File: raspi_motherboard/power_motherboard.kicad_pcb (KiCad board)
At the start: 4 copper layers, 65 x 59.5 mm, 61 parts, among them J1 GPIO, J2 Conn_02x04_Top_Bottom, J3 Conn_01x03, U1 MCP2515-xST, U2 SN65HVD230, U3 TPS563200, Y1 AMB8-12Mhz

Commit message: Add logo
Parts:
- added G***: LOGO, powerboard:krabi, F.Cu at (150.5, 94.0)
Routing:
- net GND_ELEC: vias 40 -> 41

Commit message: small fixes
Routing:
- net 12V_POW_P: track 59.4 -> 54.2 mm
- net Net-(D_12VE_INV1-K): track 21.8 -> 19.4 mm
- net GND_ELEC: track 262.8 -> 260.7 mm, vias 41 -> 49
- net 12V_ELEC_P: track 164.8 -> 162.7 mm
- net GND_POW: vias 10 -> 16
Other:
- board size 65 x 59.5 mm -> 65 x 59.9 mm

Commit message: Update
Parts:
- removed GPIO16: Conn_01x04_Socket, Connector_PinSocket_2.54mm:PinSocket_1x04_P2.54mm_Vertical
- added Tir&B: Conn_01x04_Socket, Connector_PinSocket_2.54mm:PinSocket_1x04_P2.54mm_Vertical, F.Cu at (162.8, 58.2)
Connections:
- J1 pad 38: /GPIO20/PCM.DIN -> R_IO20
- J1 pad 40: /GPIO21/PCM.DOUT -> R_IO21
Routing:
- net R_IO16: track 19.4 -> 41.8 mm
- net R_IO20: track 0.00 -> 19.0 mm
- net R_IO21: track 0.00 -> 14.4 mm
- net 3_3V: track 95.0 -> 88.5 mm
- net 5V: track 114.8 -> 108.3 mm
- net GND_ELEC: track 260.7 -> 260.2 mm, vias 49 -> 47
- net GND_POW: vias 16 -> 15

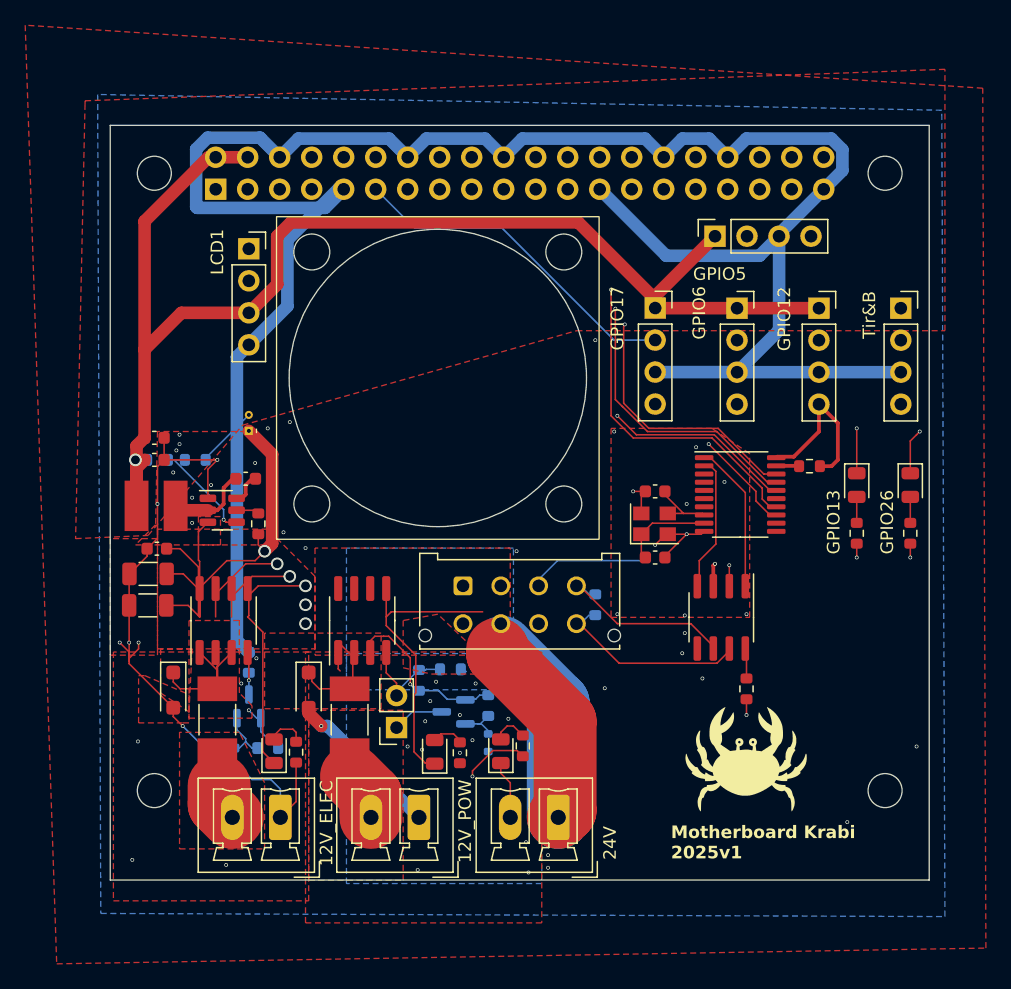
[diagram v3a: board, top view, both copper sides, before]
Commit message: fix ERC/DRC (including short-circuits) + add flood fills
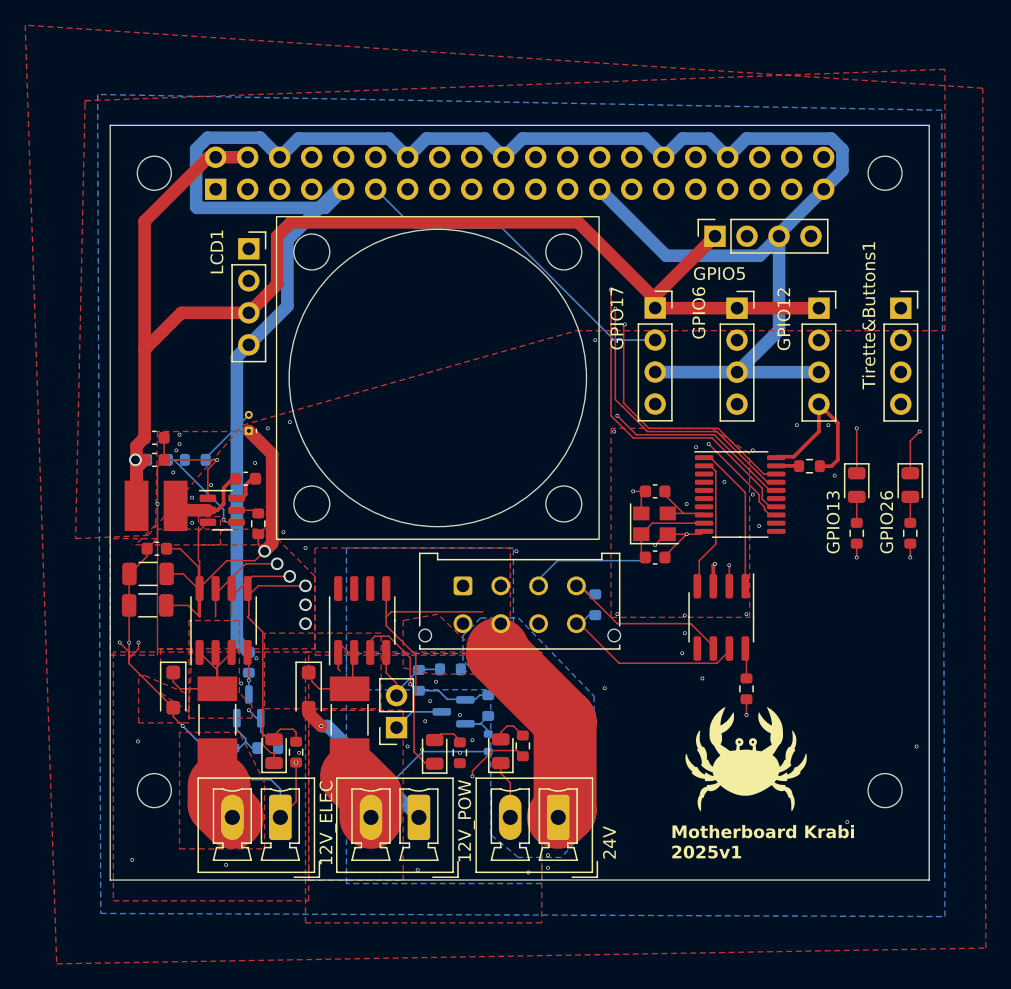
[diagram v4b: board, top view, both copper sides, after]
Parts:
- renumbered Tir&B to Tirette&Buttons1
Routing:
- net R_IO16: track 41.8 -> 22.5 mm
- net R_IO20: track 19.0 -> 38.1 mm
- net 12V_POW_P: track 54.2 -> 38.9 mm
- net 24V_POW_P: track 34.5 -> 21.9 mm
- net GND_POW: track 21.2 -> 30.3 mm, vias 15 -> 12
- net GND_ELEC: track 260.2 -> 253.7 mm, vias 47 -> 55
- added copper zone on B.Cu, net 12V_POW_P
- added copper zone on In1.Cu, net 24V_POW_P
- added copper zone on In1.Cu, net GND_ELEC
- added copper zone on In2.Cu, net GND_ELEC

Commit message: Fix double line + priority
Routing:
- net R_IO20: track 38.1 -> 19.2 mm
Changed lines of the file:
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@@
 				(polygon
 					(pts
-						(xy 111.601737 68.119259) (xy 111.499644 68.119259) (xy 111.499644 67.780494) (xy 111.601737 67.780494)
+						(xy 111.42979 67.791973) (xy 111.617369 67.791973) (xy 111.617369 68.105826) (xy 111.42979 68.105826)
 					)
 				)
@@
 	)
 	(segment
-		(start 155.1305 49.3805)
-		(end 155.1305 48.33901)
+		(start 152.82 47.5)
+		(end 151.55 46.23)
 		(width 0.127)
 		(layer "In1.Cu")
@@
 	)
 	(segment
-		(start 152.5905 47.2705)
-		(end 151.55 46.23)
+		(start 157.4165 51.6665)
+		(end 155.25 49.5)
 		(width 0.127)
 		(layer "In1.Cu")
@@
 	)
 	(segment
-		(start 157.4165 51.6665)
-		(end 155.1305 49.3805)
+		(start 157.4165 58.2065)
+		(end 157.4165 51.6665)
 		(width 0.127)
 		(layer "In1.Cu")
@@
 	)
 	(segment
-		(start 155.1305 48.33901)
-		(end 154.06199 47.2705)
+		(start 155.25 48)
+		(end 154.75 47.5)
 		(width 0.127)
 		(layer "In1.Cu")
@@
 	)
 	(segment
-		(start 157.4165 58.2065)
-		(end 157.4165 51.6665)
+		(start 162.5 63.29)
+		(end 157.4165 58.2065)
 		(width 0.127)
 		(layer "In1.Cu")
@@
 	)
 	(segment
-		(start 154.06199 47.2705)
-		(end 152.5905 47.2705)
+		(start 154.75 47.5)
+		(end 152.82 47.5)
 		(width 0.127)
 		(layer "In1.Cu")
@@
 	)
 	(segment
-		(start 162.5 63.29)
-		(end 157.4165 58.2065)
+		(start 155.25 49.5)
+		(end 155.25 48)
 		(width 0.127)
 		(layer "In1.Cu")
@@
 	)
 	(segment
-		(start 156.75 47.2705)
-		(end 155.1305 47.2705)
-		(width 0.127)
-		(layer "In1.Cu")
-		(net 25)
-	)
-	(segment
-		(start 155.1305 47.2705)
-		(end 154.09 46.23)
-		(width 0.127)
-		(layer "In1.Cu")
-		(net 25)
-	)
-	(segment
-		(start 157.6705 55.9205)
-		(end 157.6705 48.191)
-		(width 0.127)
-		(layer "In1.Cu")
-		(net 25)
-	)
-	(segment
-		(start 162.5 60.75)
-		(end 157.6705 55.9205)
-		(width 0.127)
-		(layer "In1.Cu")
-		(net 25)
-	)
-	(segment
-		(start 157.6705 48.191)
-		(end 156.75 47.2705)
-		(width 0.127)
-		(layer "In1.Cu")
-		(net 25)
-	)
-	(segment
 		(start 154.5 50.65149)
 		(end 153.0495 49.20099)
@@
 		(layer "In1.Cu")
 		(hatch edge 0.5)
-		(priority 5)
 		(connect_pads yes
 			(clearance 0)

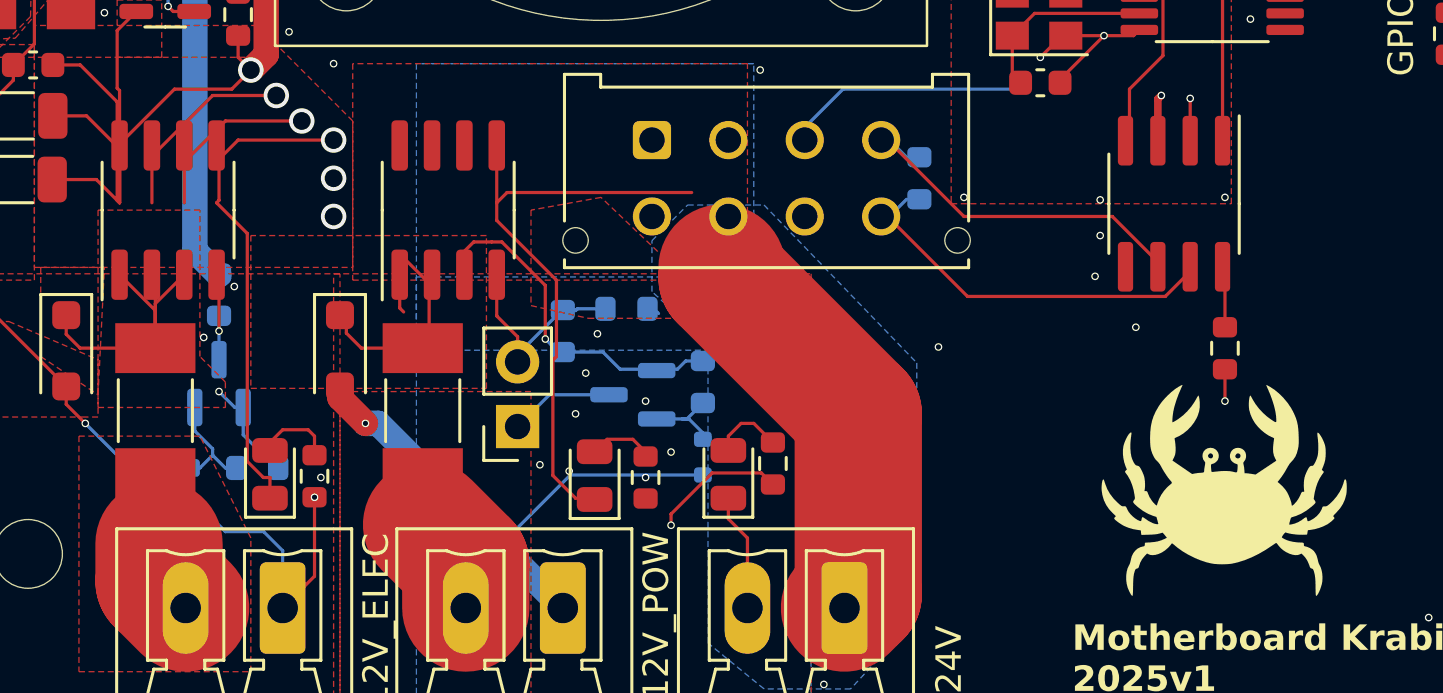
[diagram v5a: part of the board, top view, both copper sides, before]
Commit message: fix antennas (mainly on internal copper) + add labels
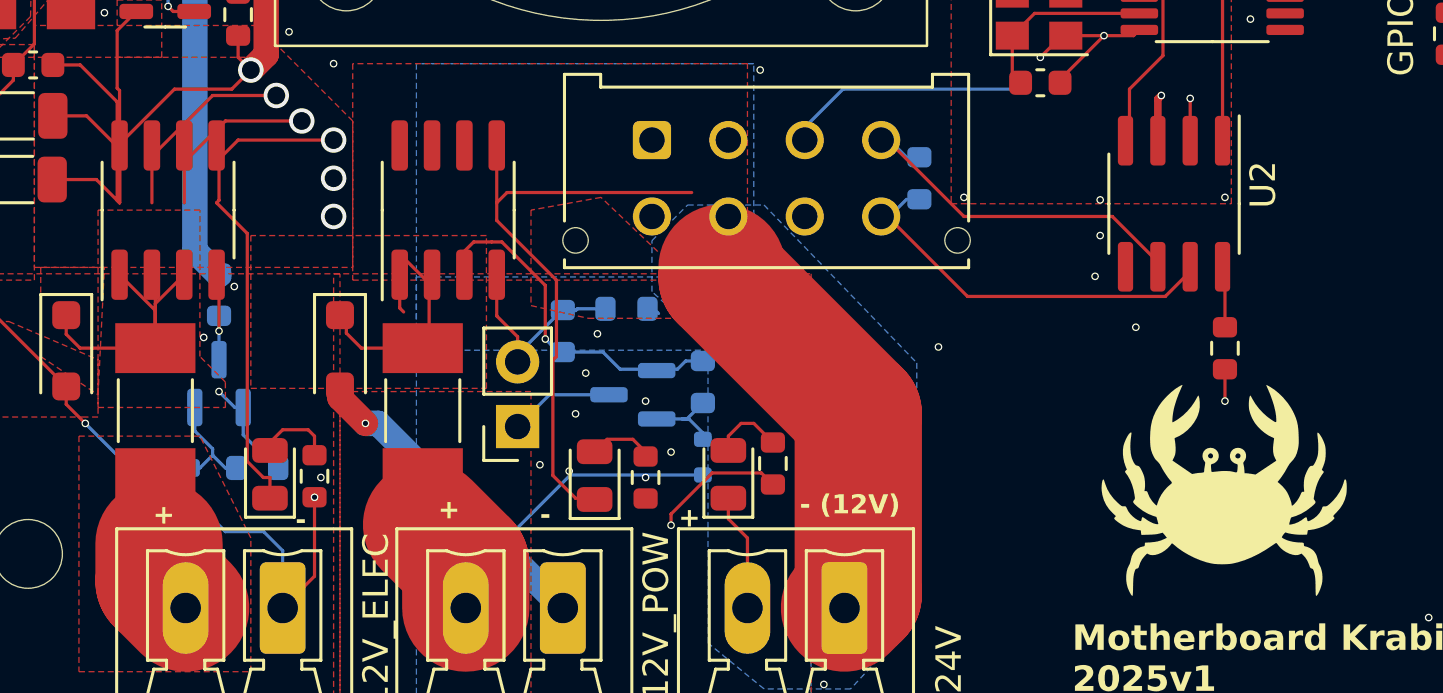
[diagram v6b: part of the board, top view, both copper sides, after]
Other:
- board text added: "+"
- board text added: "-"
- board text added: "- (12V)"

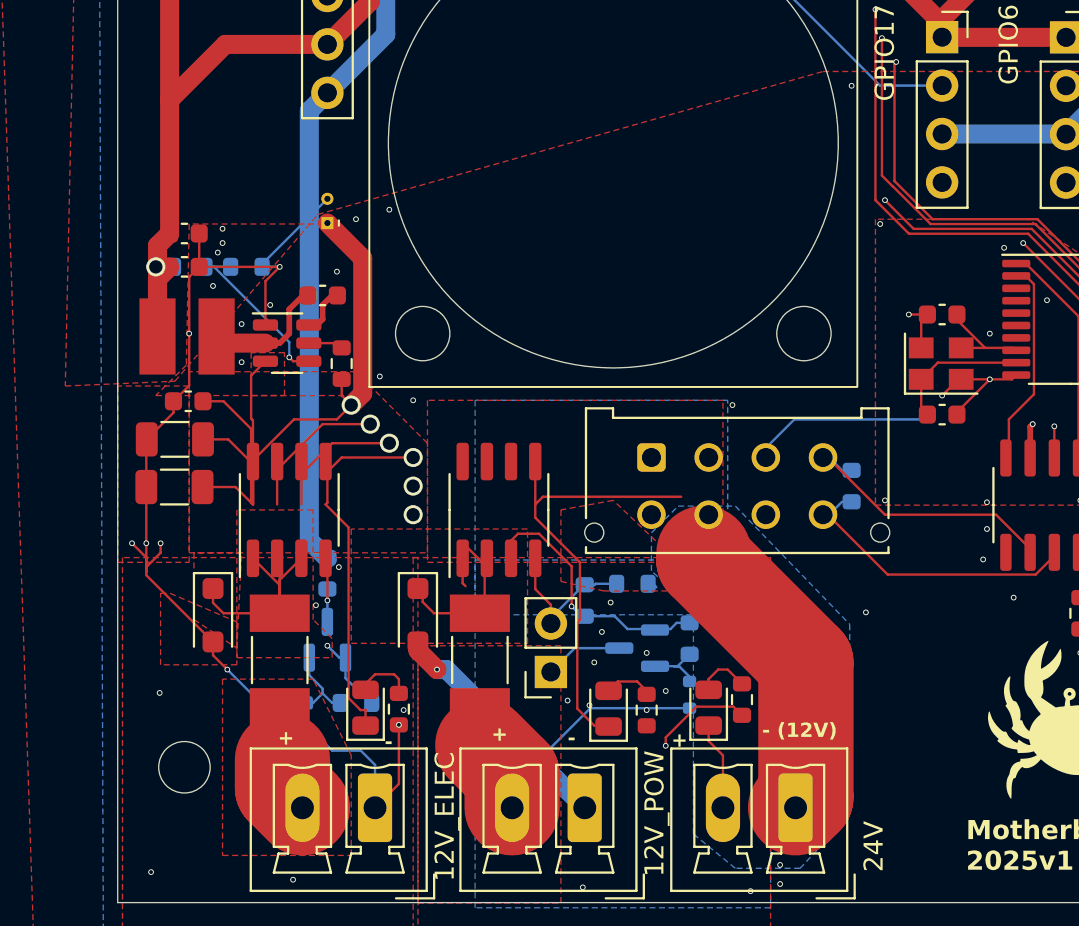
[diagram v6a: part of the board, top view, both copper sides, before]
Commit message: [WiP] start putting refs in silkscreen
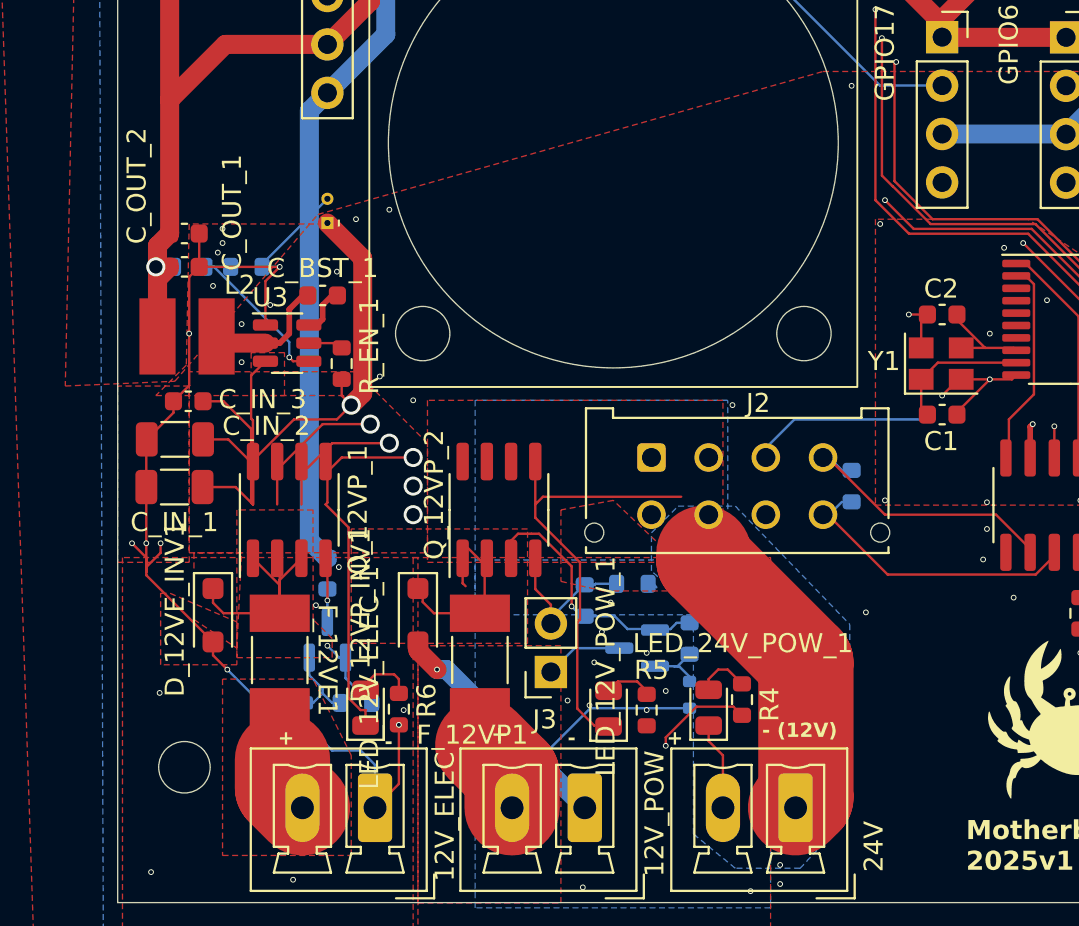
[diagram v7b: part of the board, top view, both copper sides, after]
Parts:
- renumbered R_RESET2 to R1, R_CAN1 to R2, R_RESET1 to R3, R_LED_24V_POW_1 to R4, R_LED_12V_POW_1 to R5, R_LED_12V_ELEC_1 to R6, R_LED_R_1 to R7, R_LED_R_2 to R8
